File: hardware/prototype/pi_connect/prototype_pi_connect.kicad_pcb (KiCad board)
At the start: 2 copper layers, 40 parts, among them CON1 BARREL_JACK, Q1 2N7000, Q2 2N7000, Q3 2N7000, SW1 SWITCH_INV, SW2 SWITCH_INV, SW3 SWITCH_INV, SW4 SWITCH_INV, U1 MCP23017, U2 Pi2_Connector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

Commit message: Autoroute pi_connect project, add gerber and drill files plotted with default settings.
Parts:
- moved CON1 257.9 mm to (25.4, 50.8), turned to 0 degrees
- moved R2 242.5 mm to (34.3, 151.1)
- moved C4 203.2 mm to (60.8, 143.4), turned to 90 degrees
- moved C1 196.8 mm to (68.4, 140.8), turned to 90 degrees
- moved R1 174.7 mm to (96.5, 151.1)
- moved C2 160.0 mm to (120.7, 142.2), turned to 90 degrees
- moved C3 150.8 mm to (128.3, 140.8), turned to 90 degrees
- moved U4 125.5 mm to (52.1, 137.2)
- moved U3 77.5 mm to (111.8, 137.2)
- moved R4 66.6 mm to (93.3, 71.1), turned to 0 degrees
- moved Q2 63.3 mm to (128.9, 81.3), turned to 90 degrees
- moved R3 61.9 mm to (93.3, 63.5), turned to 0 degrees
- moved R8 60.8 mm to (123.8, 71.1), turned to 0 degrees
- moved Q3 54.0 mm to (113.7, 81.3), turned to 90 degrees
- moved R5 51.8 mm to (108.6, 63.5)
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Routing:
- net VCC: track 27.9 -> 287.9 mm
- net /LEDDRIVER_CLK: track 0.00 -> 184.2 mm
- net /A_SEGC: track 0.00 -> 176.3 mm, vias 0 -> 1
- net GND: track 212.5 -> 376.5 mm
- net /A_DIG0: track 0.00 -> 155.6 mm
- net /A_SEGB: track 0.00 -> 139.2 mm
- net /B_DIG0: track 0.00 -> 133.7 mm
- net /LEDDRIVER_CS: track 14.8 -> 147.8 mm
- net /A_SEGA: track 0.00 -> 120.2 mm
- net /B_SEGG: track 0.00 -> 104.3 mm, vias 0 -> 1
- net /B_SEGDP: track 0.00 -> 99.8 mm, vias 0 -> 1
- net /A_SEGE: track 0.00 -> 97.2 mm
- net /B_SEGF: track 0.00 -> 85.4 mm
- net +3V3: track 233.0 -> 147.9 mm
- net /LEDDRIVER_CS_TTL: track 0.00 -> 72.7 mm
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- added copper zone on B.Cu, net GND
- added copper zone on F.Cu, net GND
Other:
- board outline added: 128.3 x 119.4 mm

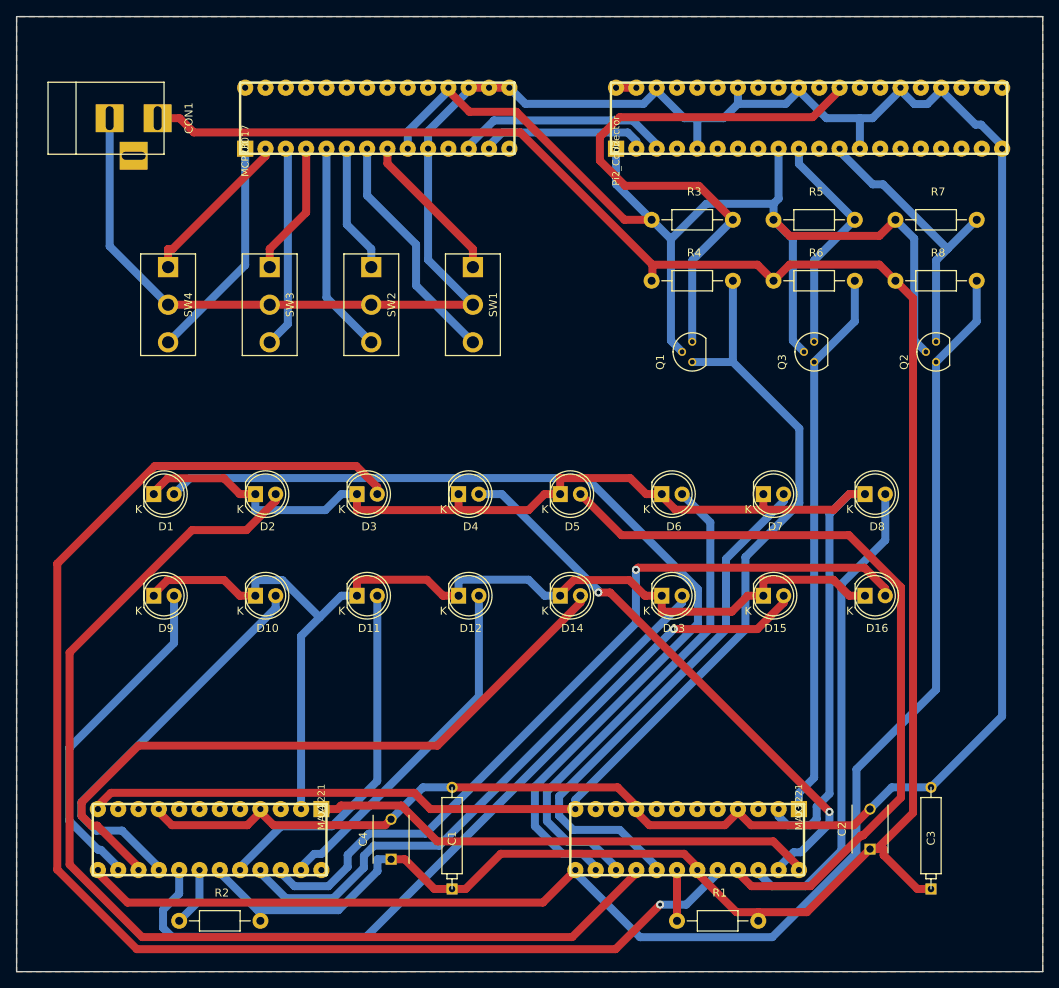
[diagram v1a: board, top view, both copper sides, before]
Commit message: Add corrected Pi connector footprint and re-route the prototype board.
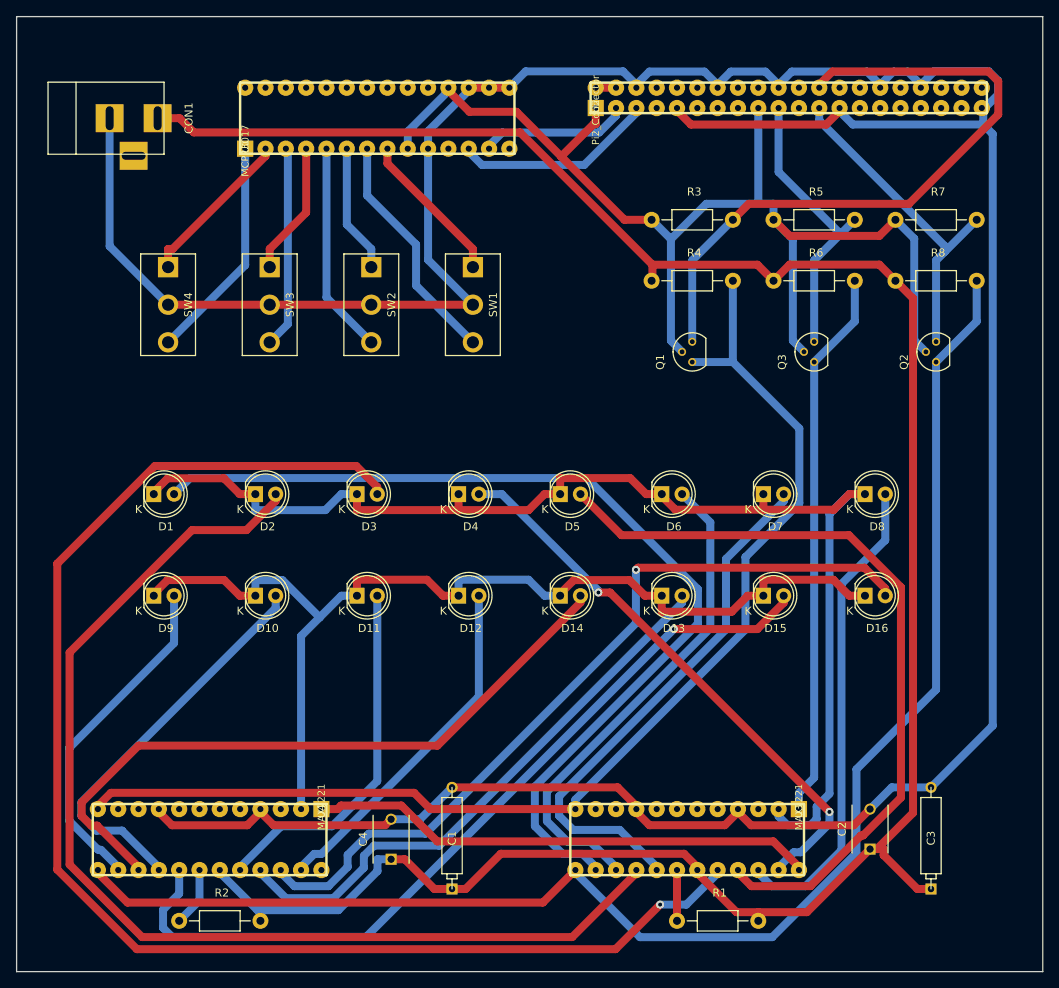
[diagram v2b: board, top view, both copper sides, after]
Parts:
- moved U2 5.68 mm to (86.4, 49.5)
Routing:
- net GND: track 376.5 -> 414.1 mm
- net /LEDDRIVER_CS_TTL: track 72.7 -> 84.1 mm
- net /LEDDRIVER_DIN_TTL: track 29.1 -> 36.3 mm
- net /LEDDRIVER_CLK_TTL: track 36.2 -> 41.8 mm
- net /IO_SDA: track 20.9 -> 18.8 mm
- net +3V3: track 147.9 -> 150.0 mm
- net /IO_SCK: track 27.0 -> 25.7 mm
- removed copper zone on B.Cu, net GND
- removed copper zone on F.Cu, net GND

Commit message: Rerouted pi connect prototype for a slightly smaller board.
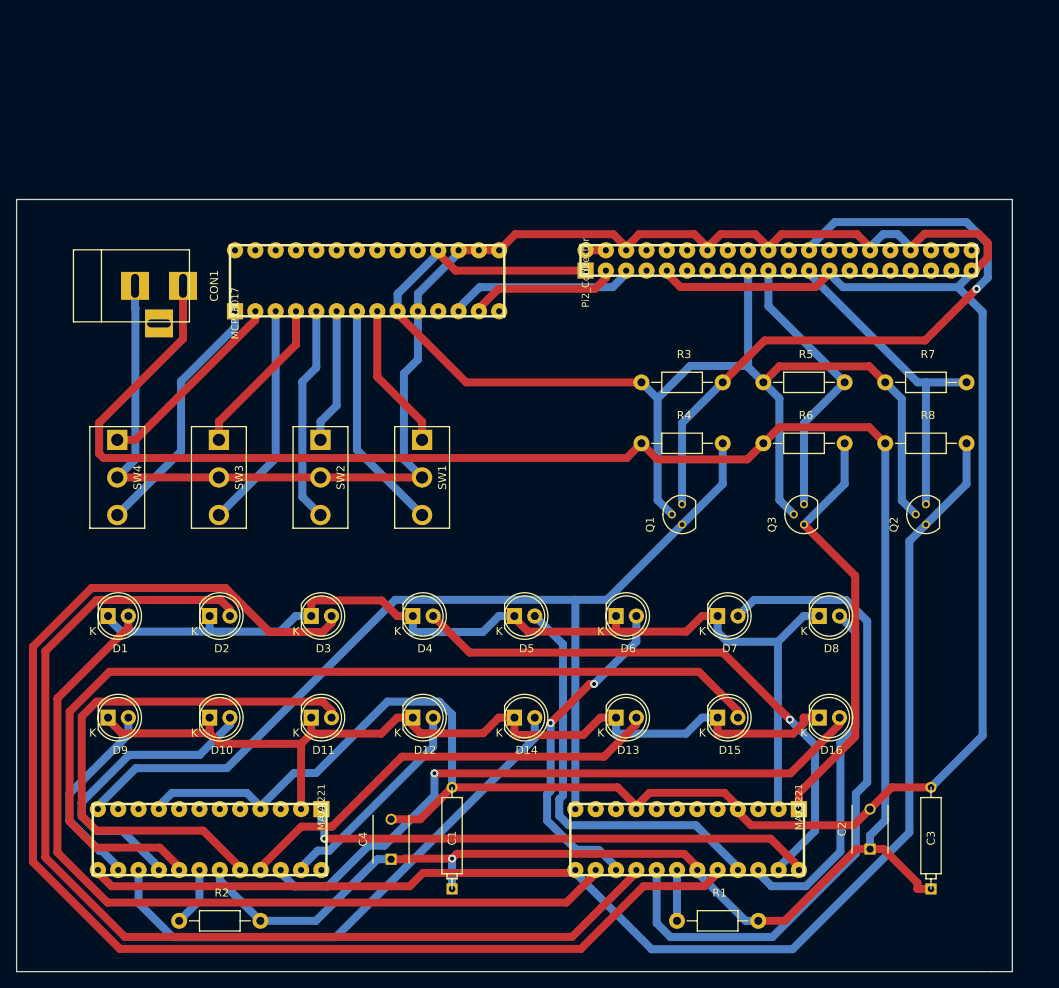
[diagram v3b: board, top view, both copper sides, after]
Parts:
- moved SW1 22.5 mm to (64.7, 95.7)
- moved SW3 22.5 mm to (39.3, 95.7)
- moved SW4 22.5 mm to (26.6, 95.7)
- moved SW2 22.5 mm to (52.0, 95.7)
- moved CON1 21.2 mm to (28.6, 71.8)
- moved U1 20.4 mm to (41.3, 74.9)
- moved Q1 20.4 mm to (97.2, 101.6)
- moved Q2 20.4 mm to (127.6, 101.6)
- moved Q3 20.4 mm to (112.4, 101.6)
- moved R3 20.4 mm to (92.1, 83.8)
- moved R4 20.4 mm to (92.1, 91.4)
- moved R5 20.4 mm to (107.3, 83.8)
- moved R6 20.4 mm to (107.3, 91.4)
- moved R7 20.4 mm to (122.6, 83.8)
- moved R8 20.4 mm to (122.6, 91.4)
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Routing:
- net /A_SEGE: track 97.2 -> 52.0 mm
- net /A_DIG0: track 155.6 -> 126.5 mm
- net /B_SEGC: track 45.1 -> 68.6 mm
- net /LEDDRIVER_CS: track 147.8 -> 126.4 mm
- net /A_SEGF: track 62.2 -> 41.9 mm, vias 0 -> 2
- net /LEDDRIVER_CLK: track 184.2 -> 165.3 mm
- net /B_DIG0: track 133.7 -> 115.5 mm
- net /B_SEGDP: track 99.8 -> 81.8 mm
- net /B_SEGA: track 42.4 -> 24.8 mm
- net /B_SEGD: track 44.0 -> 26.7 mm
- net /A_SEGG: track 67.1 -> 84.3 mm
- net /B_SEGF: track 85.4 -> 68.3 mm
- net /A_SEGDP: track 60.1 -> 44.1 mm
- net /B_SEGE: track 71.4 -> 55.6 mm
- net /LEDDRIVER_DIN: track 68.9 -> 53.4 mm
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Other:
- board size 128.3 x 119.4 mm -> 124.5 x 96.5 mm
